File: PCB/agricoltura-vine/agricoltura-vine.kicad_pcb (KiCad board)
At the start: 4 copper layers, 110 x 70 mm, 100 parts, among them SW1 TL3301NF260QG, T1 BU2032SM-JJ-GTR, T10 BM04B-SRSS-TB(LF)(SN), T11 BM04B-SRSS-TB(LF)(SN), T12 BM04B-SRSS-TB(LF)(SN), T13 BM04B-SRSS-TB(LF)(SN), T14 BM04B-SRSS-TB(LF)(SN), T15 BM04B-SRSS-TB(LF)(SN), T16 1757242, T17 0395121004, T18 0395121004, T19 TSW-108-07-G-T, T2 20021121-00010C4LF, T20 TSW-108-07-G-T, T3 0675031020, T4 BM04B-SRSS-TB(LF)(SN), T5 BM04B-SRSS-TB(LF)(SN), T6 BM04B-SRSS-TB(LF)(SN), T7 BM04B-SRSS-TB(LF)(SN), T8 BM04B-SRSS-TB(LF)(SN), T9 BM04B-SRSS-TB(LF)(SN), U1 STM32F446RET6, U2 74HC4052D, U3 TCA9548APWR, U4 AP63203WU-7, U5 AP63205WU-7, U6 MAX13450EAUD+, U7 MAX13450EAUD+, U8 SN74LV541APWR, U9 TXB0108PWR, X1 ABM3B-8.000MHZ-B2-T, X2 ABS07-32.768KHZ-9-T

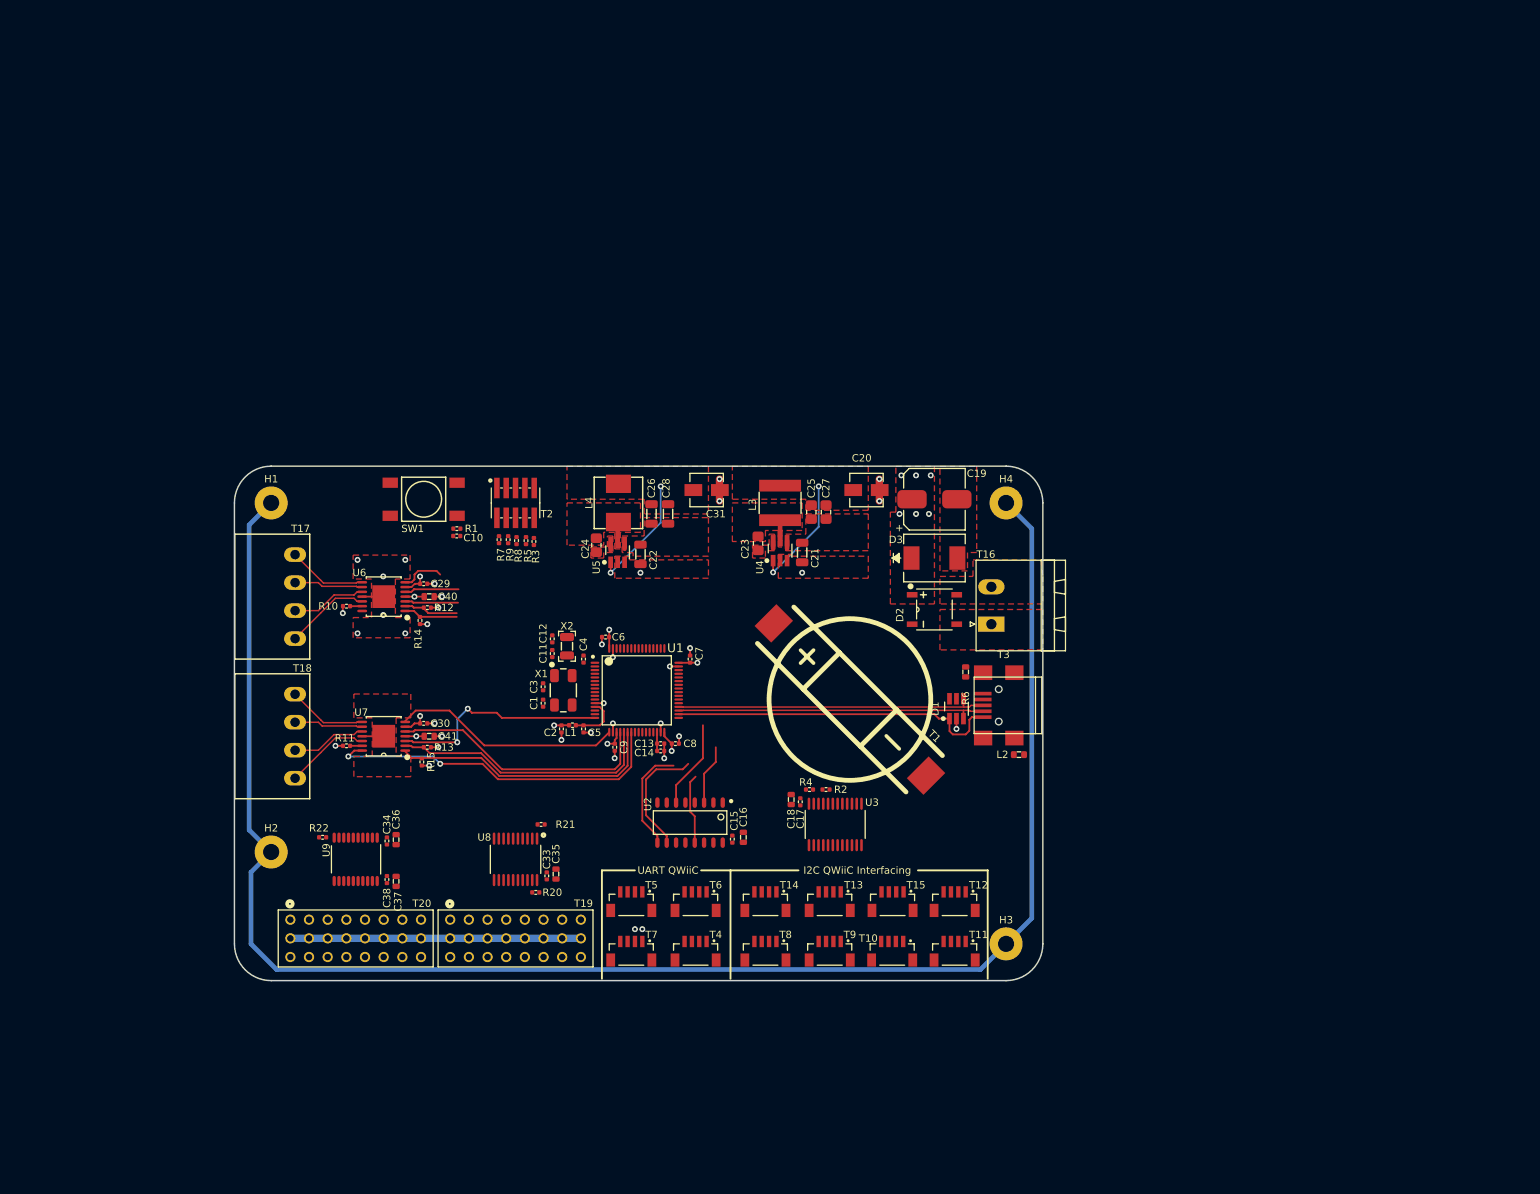
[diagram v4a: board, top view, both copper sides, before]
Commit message: Routing progress
RS845 ports routed, UART mux routed, sensor ports reoriented. Starting to come together.
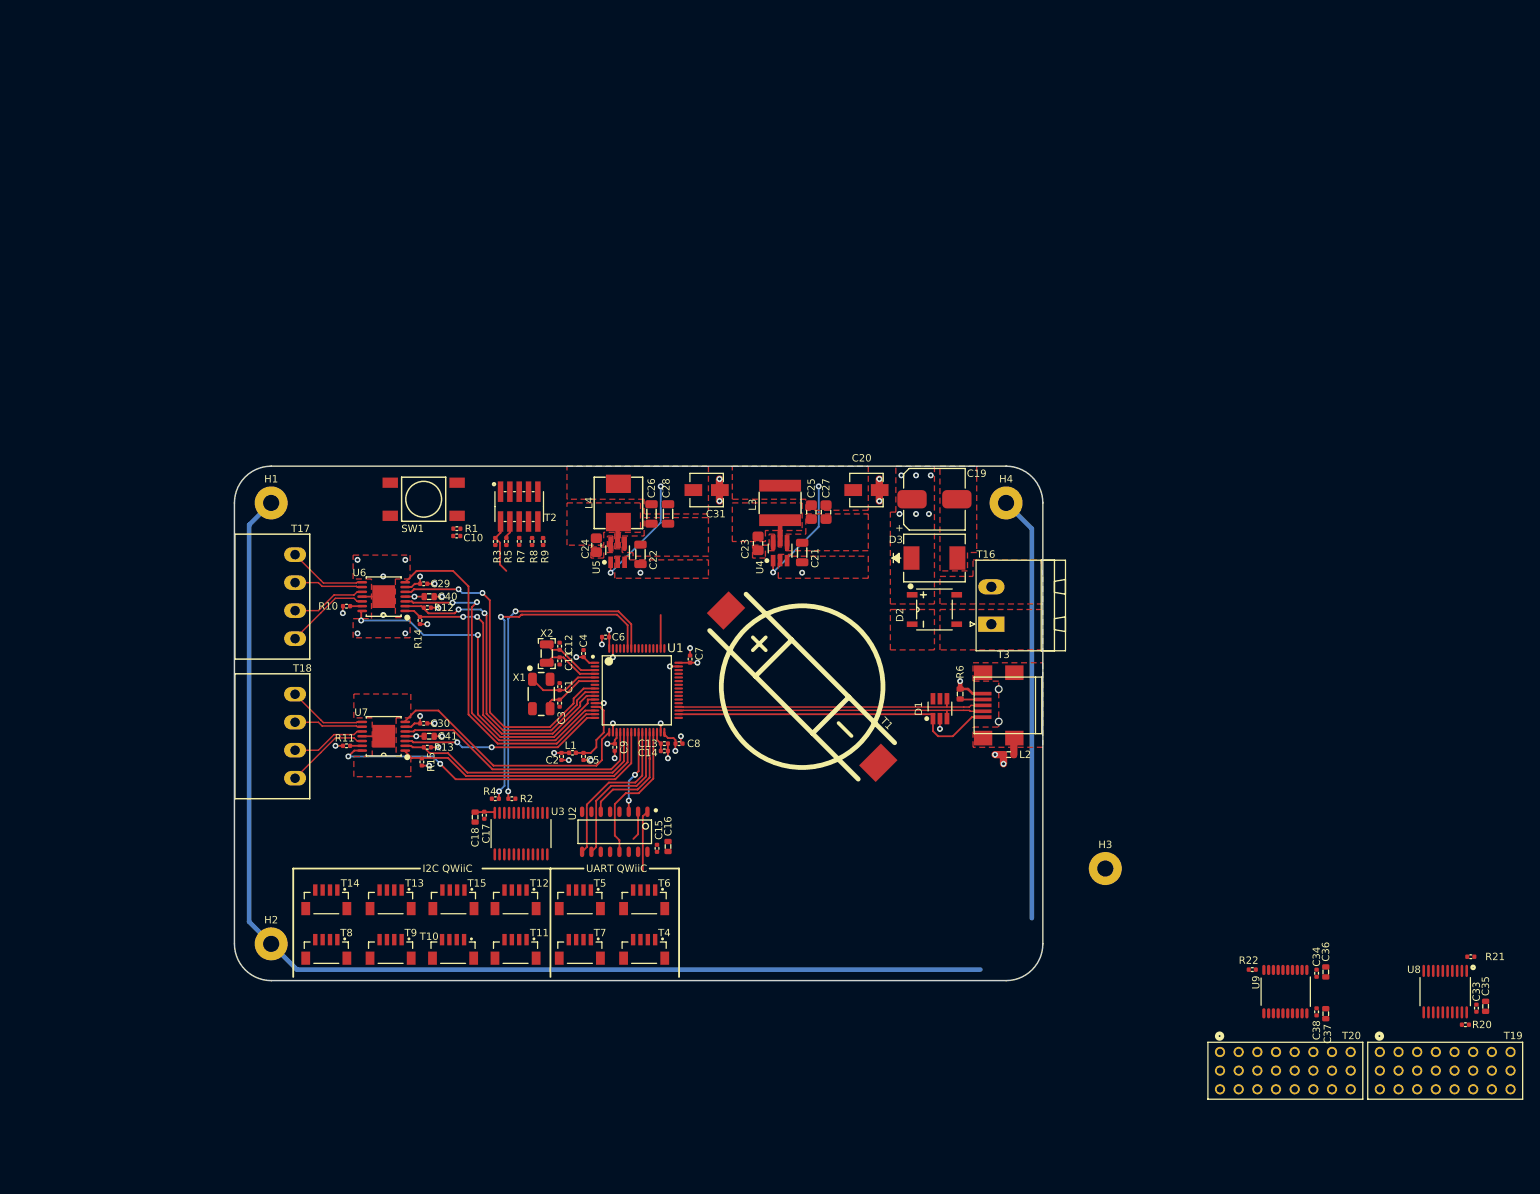
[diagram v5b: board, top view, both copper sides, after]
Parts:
- moved C33 127.8 mm to (274.0, 138.8)
- moved C34 127.8 mm to (252.2, 134.0)
- moved C35 127.8 mm to (275.2, 138.5)
- moved C36 127.8 mm to (253.5, 133.8)
- moved C37 127.8 mm to (253.5, 139.5)
- moved C38 127.8 mm to (252.2, 139.2)
- moved R20 127.8 mm to (272.5, 141.0)
- moved R21 127.8 mm to (273.2, 131.8)
- moved R22 127.8 mm to (243.5, 133.5)
- moved T19 127.8 mm to (269.8, 147.2)
- moved T20 127.8 mm to (248.0, 147.2)
- moved U8 127.8 mm to (269.8, 136.5)
- moved U9 127.8 mm to (248.0, 136.5)
- moved T10 59.8 mm to (134.8, 130.8)
- moved T11 59.8 mm to (143.2, 130.8)
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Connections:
- U1 pad 10: Net-(U1-Pad10) -> /RS485 Interface/RS485_DE1
- U1 pad 11: Net-(U1-Pad11) -> /RS485 Interface/RS485_SL_RATE1
- U1 pad 25: Net-(U1-Pad25) -> /STM32F446RET Controller/UART_SENSE1_RX
- U1 pad 26: Net-(U1-Pad26) -> /STM32F446RET Controller/USW1_S1
- U1 pad 27: Net-(U1-Pad27) -> /STM32F446RET Controller/USW1_S0
- U1 pad 28: Net-(U1-Pad28) -> /STM32F446RET Controller/USW1_EN
- U1 pad 29: Net-(U1-Pad29) -> /STM32F446RET Controller/UART_SENSE1_TX
- U1 pad 37: /STM32F446RET Controller/UART_SENSE1_TX -> Net-(U1-Pad37)
- U1 pad 38: /STM32F446RET Controller/UART_SENSE1_RX -> Net-(U1-Pad38)
- U1 pad 41: /STM32F446RET Controller/USW1_S1 -> Net-(U1-Pad41)
- U1 pad 42: /STM32F446RET Controller/USW1_EN -> Net-(U1-Pad42)
- U1 pad 43: /STM32F446RET Controller/USW1_S0 -> Net-(U1-Pad43)
- U1 pad 8: Net-(U1-Pad8) -> /RS485 Interface/RS485_TERM_EN1
- U1 pad 9: Net-(U1-Pad9) -> /RS485 Interface/RS485_RE1
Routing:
- net /RS485 Interface/RS485_SL_RATE1: track 0.00 -> 48.5 mm, vias 0 -> 2
- net /STM32F446RET Controller/I2C_SENSE1_SDA: track 0.00 -> 46.4 mm, vias 0 -> 2
- net /STM32F446RET Controller/I2C_SENSE1_SCL: track 0.00 -> 45.7 mm, vias 0 -> 2
- net /RS485 Interface/RS485_UART_RX1: track 5.99 -> 48.1 mm
- net +5V: track 60.6 -> 21.0 mm
- net /RS485 Interface/RS485_UART_TX1: track 7.26 -> 45.2 mm, vias 0 -> 2
- net /RS485 Interface/RS485_TERM_EN1: track 7.41 -> 45.2 mm, vias 0 -> 2
- net /RS485 Interface/RS485_RE1: track 7.41 -> 43.6 mm, vias 0 -> 2
- net /RS485 Interface/RS485_DE1: track 7.34 -> 42.5 mm, vias 0 -> 2
- net Earth: track 232.2 -> 218.4 mm
- net /STM32F446RET Controller/UART_SENSE1_TX: track 9.54 -> 19.7 mm
- net /STM32F446RET Controller/OSC_IN: track 0.00 -> 9.83 mm
- net /STM32F446RET Controller/OSC_OUT: track 0.00 -> 8.66 mm
- net /UART Sensor Interfaces/UARTS1_RX: track 0.00 -> 8.30 mm
- net /STM32F446RET Controller/OSC32_IN: track 0.00 -> 8.00 mm
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- added copper zone on F.Cu, net Net-(L2-Pad1)
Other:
- board text added: "I2C QWiiC"
- board text removed: "I2C QWiiC Interfacing"

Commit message: Majopr Progress
Board shape enlarged to simplify layout and accomodate larger size parts for sisterboard like Ivy. QWIIC connectors flipped to be correct, signals were oriented incorrectly in past revisions.
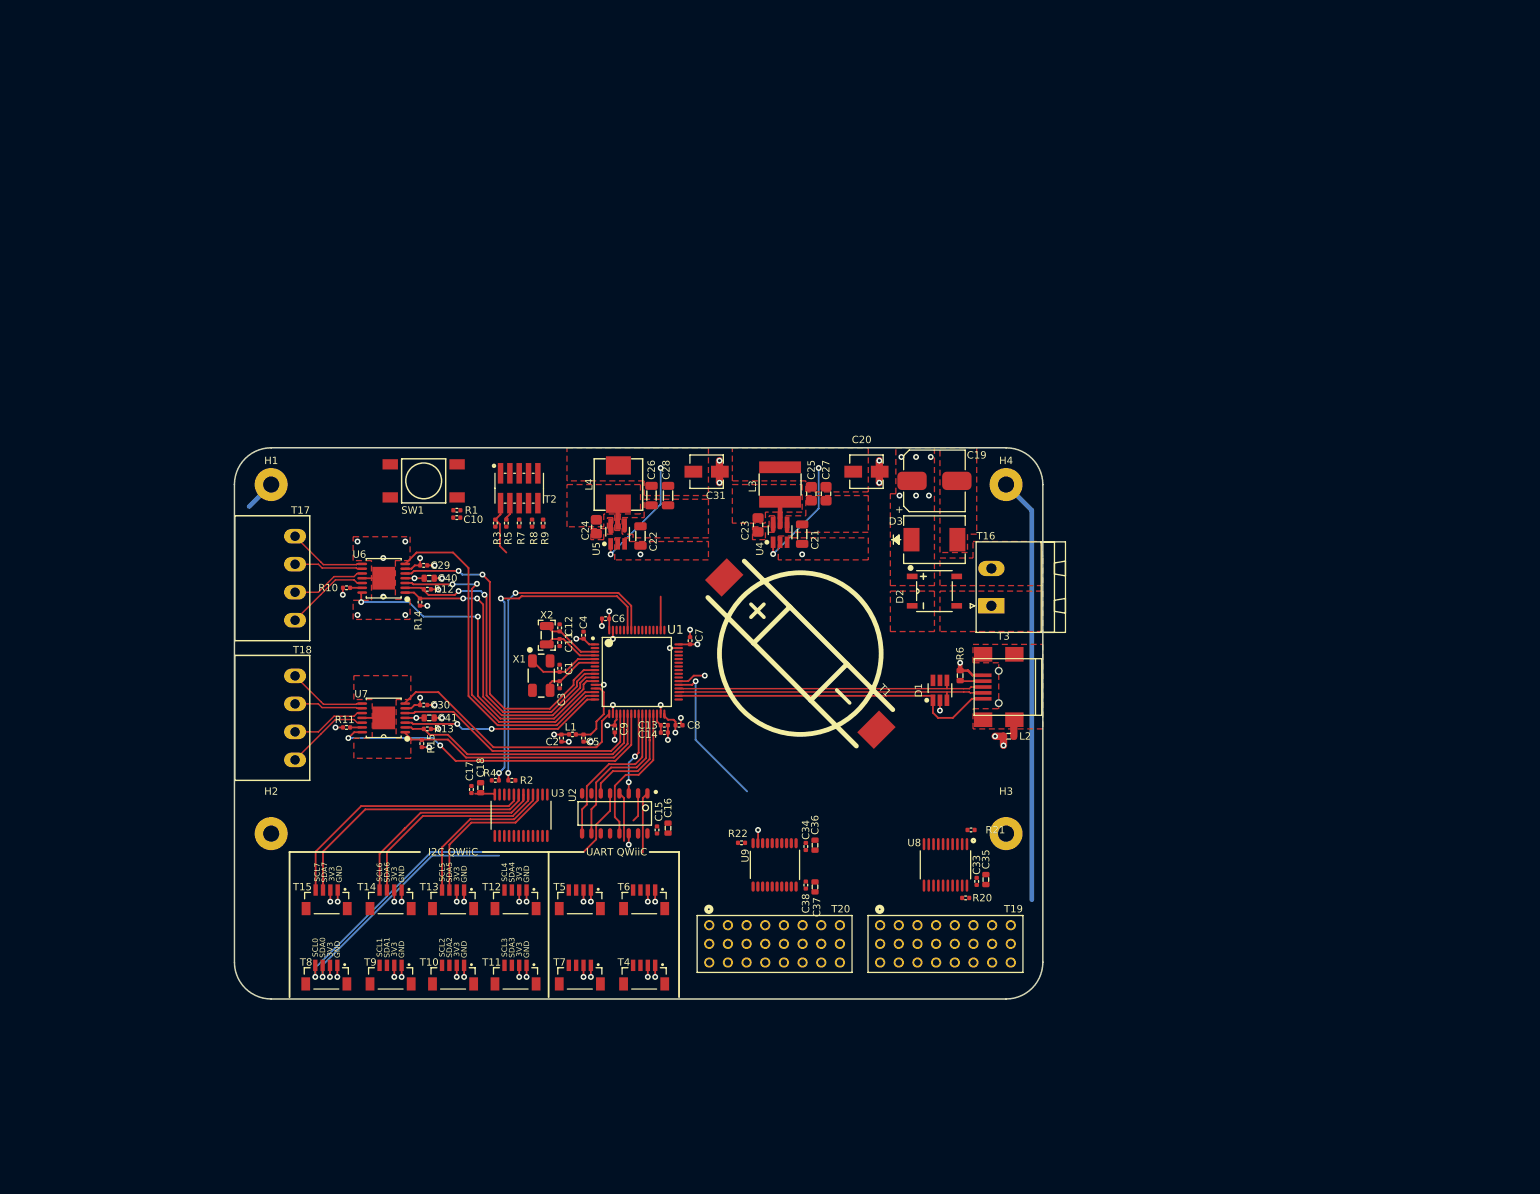
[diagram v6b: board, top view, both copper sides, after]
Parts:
- moved C34 71.6 mm to (182.8, 116.8)
- moved C36 71.6 mm to (184.0, 116.6)
- moved C37 71.6 mm to (184.0, 122.2)
- moved C38 71.6 mm to (182.8, 122.0)
- moved R22 71.6 mm to (174.0, 116.2)
- moved T20 71.6 mm to (178.5, 130.0)
- moved U9 71.6 mm to (178.5, 119.2)
- moved C33 70.2 mm to (206.0, 121.5)
- moved C35 70.2 mm to (207.2, 121.2)
- moved R20 70.2 mm to (204.5, 123.8)
- moved R21 70.2 mm to (205.2, 114.5)
- moved T19 70.2 mm to (201.8, 130.0)
- moved U8 70.2 mm to (201.8, 119.2)
- moved H2 17.5 mm to (110.0, 112.5)
- moved T15 17.3 mm to (117.5, 124.0)
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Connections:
- net Net-(U9-Pad1) renamed /5V IO Interfaces/5VGPIO_BD_0
- net Net-(U9-Pad3) renamed /5V IO Interfaces/5VGPIO_BD_1
- net Net-(U9-Pad4) renamed /5V IO Interfaces/5VGPIO_BD_2
- net Net-(U9-Pad5) renamed /5V IO Interfaces/5VGPIO_BD_3
- net Net-(U9-Pad6) renamed /5V IO Interfaces/5VGPIO_BD_4
- net Net-(U9-Pad7) renamed /5V IO Interfaces/5VGPIO_BD_5
- net Net-(U9-Pad8) renamed /5V IO Interfaces/5VGPIO_BD_6
- T10 pad 1: Net-(T10-Pad1) -> GND
- T10 pad 2: Net-(T10-Pad2) -> +3V3
- T10 pad 3: +3V3 -> /I2C Sensor Interfaces/QWIIC_SD2
- T10 pad 4: GND -> /I2C Sensor Interfaces/QWIIC_SC2
- T11 pad 1: Net-(T11-Pad1) -> GND
- T11 pad 2: Net-(T11-Pad2) -> +3V3
- T11 pad 3: +3V3 -> /I2C Sensor Interfaces/QWIIC_SD3
- T11 pad 4: GND -> /I2C Sensor Interfaces/QWIIC_SC3
- T12 pad 1: Net-(T12-Pad1) -> GND
- T12 pad 2: Net-(T12-Pad2) -> +3V3
- T12 pad 3: +3V3 -> /I2C Sensor Interfaces/QWIIC_SD4
- T12 pad 4: GND -> /I2C Sensor Interfaces/QWIIC_SC4
- T13 pad 1: Net-(T13-Pad1) -> GND
- T13 pad 2: Net-(T13-Pad2) -> +3V3
- T13 pad 3: +3V3 -> /I2C Sensor Interfaces/QWIIC_SD5
- T13 pad 4: GND -> /I2C Sensor Interfaces/QWIIC_SC5
- T14 pad 1: Net-(T14-Pad1) -> GND
- T14 pad 2: Net-(T14-Pad2) -> +3V3
- T14 pad 3: +3V3 -> /I2C Sensor Interfaces/QWIIC_SD6
- T14 pad 4: GND -> /I2C Sensor Interfaces/QWIIC_SC6
- T15 pad 1: Net-(T15-Pad1) -> GND
- T15 pad 2: Net-(T15-Pad2) -> +3V3
- T15 pad 3: +3V3 -> /I2C Sensor Interfaces/QWIIC_SD7
- T15 pad 4: GND -> /I2C Sensor Interfaces/QWIIC_SC7
- T4 pad 1: /UART Sensor Interfaces/UARTS1_RX -> GND
- T4 pad 2: /UART Sensor Interfaces/UARTS1_TX -> +3V3
- T4 pad 3: +3V3 -> /UART Sensor Interfaces/UARTS1_TX
- T4 pad 4: GND -> /UART Sensor Interfaces/UARTS1_RX
- T5 pad 1: /UART Sensor Interfaces/UARTS2_RX -> GND
- T5 pad 2: /UART Sensor Interfaces/UARTS2_TX -> +3V3
- T5 pad 3: +3V3 -> /UART Sensor Interfaces/UARTS2_TX
- T5 pad 4: GND -> /UART Sensor Interfaces/UARTS2_RX
- T6 pad 1: /UART Sensor Interfaces/UARTS3_RX -> GND
- T6 pad 2: /UART Sensor Interfaces/UARTS3_TX -> +3V3
- T6 pad 3: +3V3 -> /UART Sensor Interfaces/UARTS3_TX
- T6 pad 4: GND -> /UART Sensor Interfaces/UARTS3_RX
- T7 pad 1: /UART Sensor Interfaces/UARTS4_RX -> GND
- T7 pad 2: /UART Sensor Interfaces/UARTS4_TX -> +3V3
- T7 pad 3: +3V3 -> /UART Sensor Interfaces/UARTS4_TX
- T7 pad 4: GND -> /UART Sensor Interfaces/UARTS4_RX
- T8 pad 1: Net-(T8-Pad1) -> GND
- T8 pad 2: Net-(T8-Pad2) -> +3V3
- T8 pad 3: +3V3 -> /I2C Sensor Interfaces/QWIIC_SD0
- T8 pad 4: GND -> /I2C Sensor Interfaces/QWIIC_SC0
- T9 pad 1: Net-(T9-Pad1) -> GND
- T9 pad 2: Net-(T9-Pad2) -> +3V3
- T9 pad 3: +3V3 -> /I2C Sensor Interfaces/QWIIC_SD1
- T9 pad 4: GND -> /I2C Sensor Interfaces/QWIIC_SC1
- U1 pad 37: Net-(U1-Pad37) -> /5V IO Interfaces/5VGPIO_BD_7
- U3 pad 10: Net-(T11-Pad2) -> /I2C Sensor Interfaces/QWIIC_SD3
- U3 pad 11: Net-(T11-Pad1) -> /I2C Sensor Interfaces/QWIIC_SC3
- U3 pad 13: Net-(T12-Pad2) -> /I2C Sensor Interfaces/QWIIC_SD4
- U3 pad 14: Net-(T12-Pad1) -> /I2C Sensor Interfaces/QWIIC_SC4
- U3 pad 15: Net-(T13-Pad2) -> /I2C Sensor Interfaces/QWIIC_SD5
- U3 pad 16: Net-(T13-Pad1) -> /I2C Sensor Interfaces/QWIIC_SC5
- U3 pad 17: Net-(T14-Pad2) -> /I2C Sensor Interfaces/QWIIC_SD6
- U3 pad 18: Net-(T14-Pad1) -> /I2C Sensor Interfaces/QWIIC_SC6
- U3 pad 19: Net-(T15-Pad2) -> /I2C Sensor Interfaces/QWIIC_SD7
- U3 pad 20: Net-(T15-Pad1) -> /I2C Sensor Interfaces/QWIIC_SC7
- U3 pad 4: Net-(T8-Pad2) -> /I2C Sensor Interfaces/QWIIC_SD0
- U3 pad 5: Net-(T8-Pad1) -> /I2C Sensor Interfaces/QWIIC_SC0
- U3 pad 6: Net-(T9-Pad2) -> /I2C Sensor Interfaces/QWIIC_SD1
- U3 pad 7: Net-(T9-Pad1) -> /I2C Sensor Interfaces/QWIIC_SC1
- U3 pad 8: Net-(T10-Pad2) -> /I2C Sensor Interfaces/QWIIC_SD2
- U3 pad 9: Net-(T10-Pad1) -> /I2C Sensor Interfaces/QWIIC_SC2
- U9 pad 9: Net-(U9-Pad9) -> /5V IO Interfaces/5VGPIO_BD_7
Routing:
- net Earth: track 218.4 -> 62.2 mm
- net /I2C Sensor Interfaces/QWIIC_SC7: track 0.00 -> 35.9 mm
- net /I2C Sensor Interfaces/QWIIC_SC0: track 0.00 -> 35.8 mm, vias 0 -> 1
- net /I2C Sensor Interfaces/QWIIC_SD7: track 0.00 -> 35.6 mm
- net /I2C Sensor Interfaces/QWIIC_SD0: track 0.00 -> 33.4 mm, vias 0 -> 1
- net /I2C Sensor Interfaces/QWIIC_SC6: track 0.00 -> 28.7 mm
- net /I2C Sensor Interfaces/QWIIC_SD6: track 0.00 -> 28.1 mm
- net /5V IO Interfaces/5VGPIO_BD_7: track 0.00 -> 22.2 mm, vias 0 -> 2
- net /I2C Sensor Interfaces/QWIIC_SC5: track 0.00 -> 21.6 mm
- net /I2C Sensor Interfaces/QWIIC_SD5: track 0.00 -> 21.5 mm
- net +3V3: track 43.2 -> 62.1 mm, vias 13 -> 25
- net GND: track 42.3 -> 61.2 mm, vias 32 -> 44
- net /UART Sensor Interfaces/UARTS2_TX: track 0.00 -> 9.47 mm
- net /UART Sensor Interfaces/UARTS4_TX: track 0.00 -> 6.72 mm
- net Net-(U1-Pad38): track 0.00 -> 3.86 mm, vias 0 -> 1
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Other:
- board size 110 x 70 mm -> 110 x 75 mm
- board text added: "3V3"
- board text added: "GND"
- board text added: "SCL0"
- board text added: "SCL1"
- board text added: "SCL2"
- board text added: "SCL3"
- board text added: "SCL4"
- board text added: "SCL5"
- board text added: "SCL6"
- board text added: "SCL7"
- board text added: "SDA0"
- board text added: "SDA1"
- board text added: "SDA2"
- board text added: "SDA3"
- board text added: "SDA4"
- board text added: "SDA5"
- board text added: "SDA6"
- board text added: "SDA7"
